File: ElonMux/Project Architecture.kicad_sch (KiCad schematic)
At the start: 0 parts

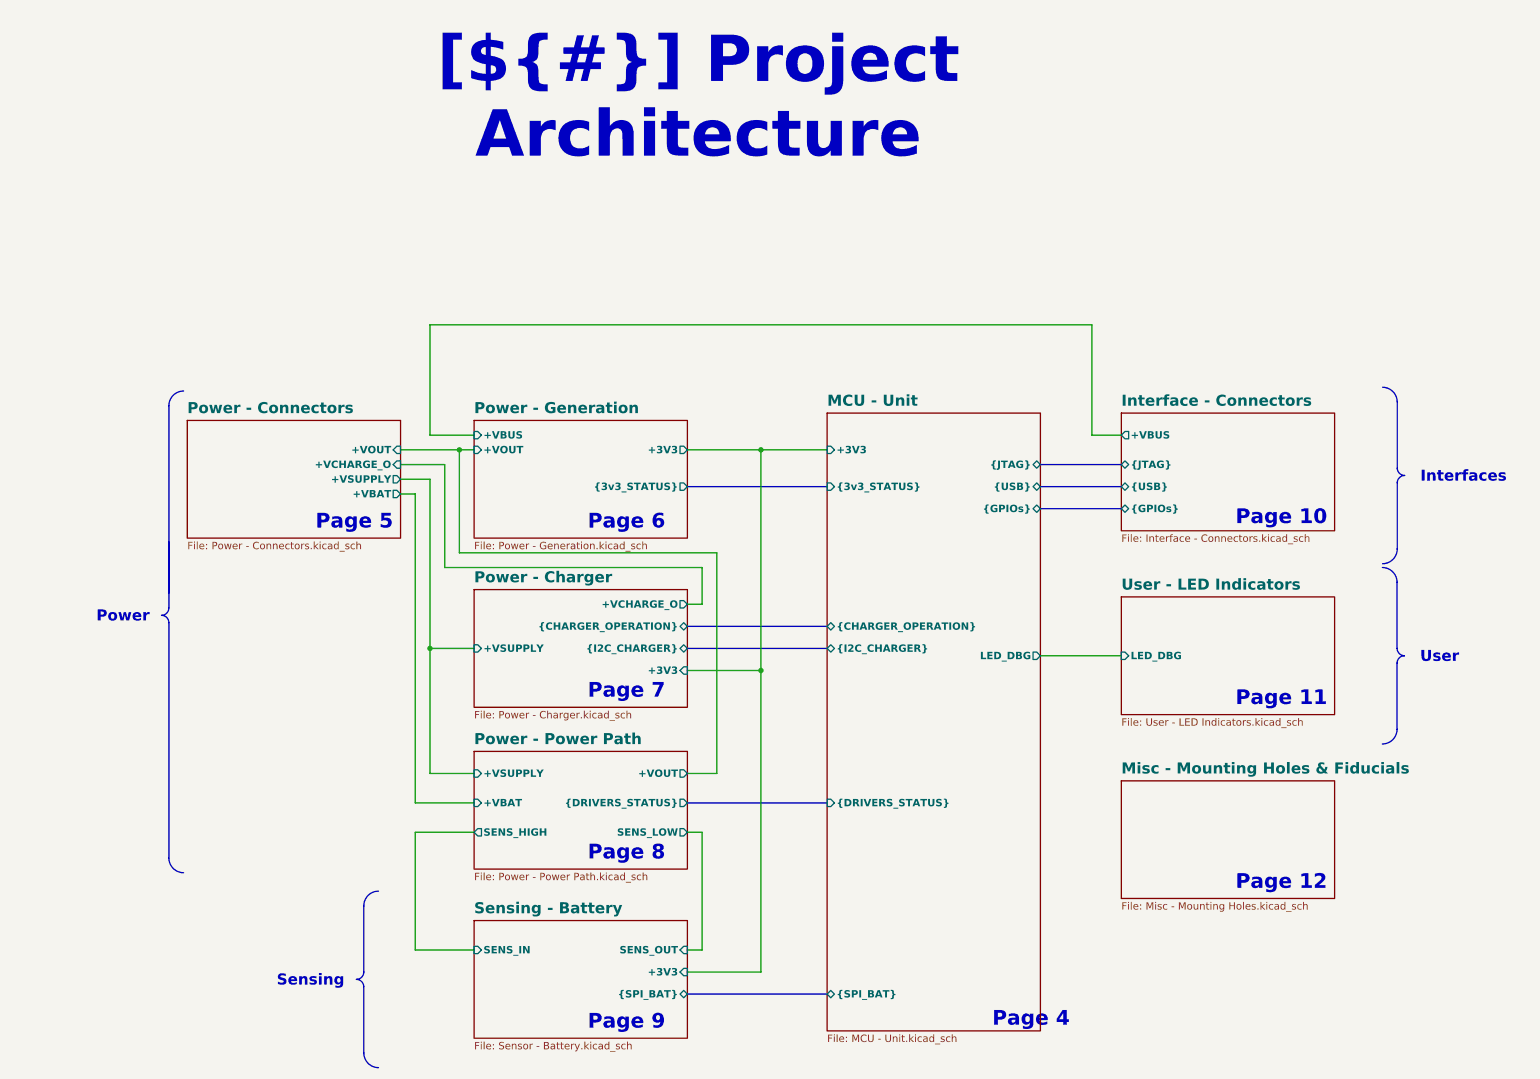
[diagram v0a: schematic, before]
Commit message: Done with changes of v1.1, need to final check and order
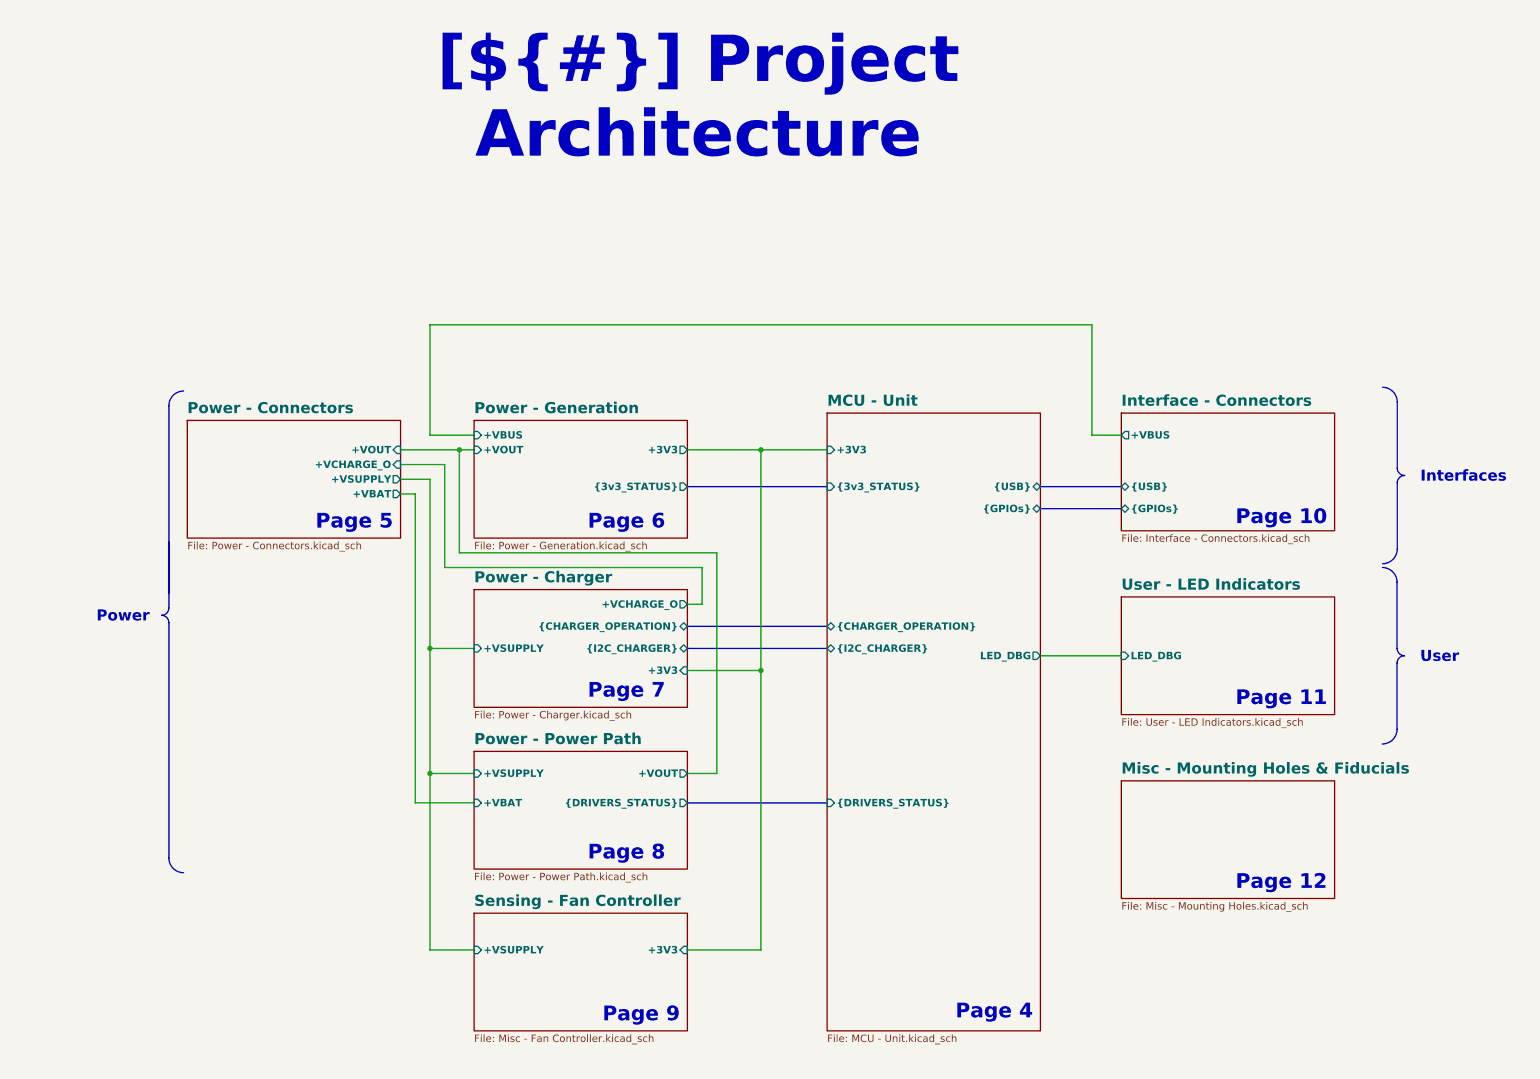
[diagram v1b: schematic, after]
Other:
- removed sheet Sensing - Battery
- added sheet Sensing - Fan Controller (Misc - Fan Controller.kicad_sch)
- sheet Interface - Connectors ports: added none; removed {JTAG}
- sheet MCU - Unit ports: added none; removed {JTAG}, {SPI_BAT}
- sheet Power - Power Path ports: added none; removed SENS_HIGH, SENS_LOW

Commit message: Finished V1.1, maybe extra cleaning needed of some details in the doc
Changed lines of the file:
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@@
 	(title_block
 		(title "Project Architecture")
-		(date "2025-06-17")
+		(date "2025-07-24")
 		(rev "${REVISION}")
 		(company "${COMPANY}")
@@
 	)
 	(arc
+		(start 118.72 164.495)
+		(mid 119.4642 162.7007)
+		(end 121.26 161.955)
+		(stroke
+			(width 0)
+			(type default)
+		)
+		(fill
+			(type none)
+		)
+	)
+	(arc
 		(start 332.095 123.18)
 		(mid 331.2031 122.8034)
@@
 	)
 	(arc
+		(start 117.45 177.195)
+		(mid 118.3419 177.5716)
+		(end 118.72 178.465)
+		(stroke
+			(width 0)
+			(type default)
+		)
+		(fill
+			(type none)
+		)
+	)
+	(arc
 		(start 332.13 92.055)
 		(mid 331.2395 91.677)
@@
 	)
 	(arc
+		(start 118.72 175.925)
+		(mid 118.3454 176.8219)
+		(end 117.45 177.195)
+		(stroke
+			(width 0)
+			(type default)
+		)
+		(fill
+			(type none)
+		)
+	)
+	(arc
 		(start 330.825 135.88)
 		(mid 330.0808 137.6743)
@@
 	)
 	(arc
+		(start 121.26 192.435)
+		(mid 119.4729 191.6835)
+		(end 118.72 189.895)
+		(stroke
+			(width 0)
+			(type default)
+		)
+		(fill
+			(type none)
+		)
+	)
+	(arc
 		(start 118.745 80.01)
 		(mid 119.4886 78.2122)
@@
 			)
 			(justify right top)
+		)
+	)
+	(text_box "Sensing"
+		(exclude_from_sim no)
+		(at 90.155 174.625 0)
+		(size 26.015 5.1)
+		(margins 1.4287 1.4287 1.4287 1.4287)
+		(stroke
+			(width -0.0001)
+			(type solid)
+		)
+		(fill
+			(type none)
+		)
+		(effects
+			(font
+				(size 1.905 1.905)
+				(thickness 0.381)
+				(bold yes)
+				(color 0 0 0 1)
+			)
+			(justify left top)
 		)
 	)
@@
 		)
 	)
+	(polyline
+		(pts
+			(xy 118.72 178.465) (xy 118.72 189.895)
+		)
+		(stroke
+			(width 0)
+			(type default)
+		)
+	)
 	(wire
 		(pts
@@
 		)
 		(stroke
+			(width 0)
+			(type default)
+		)
+	)
+	(polyline
+		(pts
+			(xy 118.72 175.925) (xy 118.72 164.495)
+		)
+		(stroke
